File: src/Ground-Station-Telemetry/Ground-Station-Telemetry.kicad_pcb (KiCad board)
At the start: 4 copper layers, 94.9 x 43.2 mm, 47 parts, among them J1 Jumper_NO, P1 3220-20-0200-00, P2 USB, U1 STM32H750VBTx, U2 LMS8117AMP-3.3_NOPB, U3 CP2102-GMR(QFN28), U4 RFM95W-868S2, U5 XB24CDMPIT-001, Y1 ECS-240-18-33-JGN-TR

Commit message: finished initial rev 2 routing
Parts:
- removed H3: Mounting-Hole, Engine-Controller:MountingHole_4.3mm_M4_DIN965
- added C19: 0.1uF, Ground-Station-Telemetry:CAP_0603, F.Cu at (190.5, 82.8)
- added D5: SMBJ36CA-13-F, Ground-Station-Telemetry:CDSOT23-SM712, F.Cu at (207.5, 83.6)
- added D6: SMBJ36CA-13-F, Ground-Station-Telemetry:CDSOT23-SM712, F.Cu at (207.9, 89.2)
- added P3: 54602-908LF, Ground-Station-Telemetry:54602-908LF, F.Cu at (214.6, 86.7)
- added R10: 10, Ground-Station-Telemetry:RES_0603, F.Cu at (200.9, 83.1)
- added R11: 100, Ground-Station-Telemetry:RES_0603, F.Cu at (204.1, 83.7)
- added R12: 10, Ground-Station-Telemetry:RES_0603, F.Cu at (200.9, 85.7)
- added R13: 10, Ground-Station-Telemetry:RES_0603, F.Cu at (200.9, 88.4)
- added R14: 100, Ground-Station-Telemetry:RES_0603, F.Cu at (204.5, 89.0)
- added R15: 10, Ground-Station-Telemetry:RES_0603, F.Cu at (200.9, 90.2)
- added U6: SN65HVD71DR, Ground-Station-Telemetry:SN65HVD71DR, F.Cu at (194.6, 86.9)
- moved R6 30.0 mm to (185.7, 84.8), turned to 180 degrees
- moved D2 29.4 mm to (185.5, 80.9)
- moved R5 13.7 mm to (215.9, 111.8), turned to -90 degrees
- moved R4 10.0 mm to (213.4, 111.8), turned to -90 degrees
- moved C4 8.44 mm to (202.1, 77.4)
- moved R7 8.24 mm to (179.6, 74.3)
- moved D3 7.71 mm to (185.3, 75.3)
- moved C7 7.35 mm to (190.0, 77.7)
- moved U2 7.35 mm to (196.3, 77.0)
- moved P2 4.46 mm to (214.9, 100.2)
- moved C16 3.39 mm to (203.1, 97.4)
- moved C17 3.37 mm to (201.3, 97.4)
- moved D4 3.18 mm to (206.2, 102.5)
- moved U3 2.53 mm to (198.2, 102.1)
- moved R8 2.29 mm to (196.8, 95.4)
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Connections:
- D4 pad 4: 5V -> unconnected-(D4-Pad4)
- D4 pad 5: unconnected-(D4-Pad5) -> 5V
- U1 pad 51: unconnected-(U1-Pad51) -> RS485_RX
- U1 pad 52: unconnected-(U1-Pad52) -> RS485_TX
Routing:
- net RS485_RX: track 0.00 -> 23.2 mm, vias 0 -> 2
- net Y: track 0.00 -> 21.4 mm, vias 0 -> 1
- net RS485_TX: track 0.00 -> 20.0 mm, vias 0 -> 2
- net Z: track 0.00 -> 18.2 mm, vias 0 -> 1
- net B: track 0.00 -> 13.3 mm
- net SWCLK: track 31.3 -> 44.2 mm
- net A: track 0.00 -> 11.5 mm
- net 5V: track 52.5 -> 62.1 mm, vias 1 -> 2
- net SWDIO: track 29.6 -> 37.5 mm
- net 3.3V: track 65.7 -> 72.6 mm, vias 11 -> 14
- net Net-(U6-A): track 0.00 -> 3.75 mm
- net Net-(U6-Y): track 0.00 -> 3.32 mm
- net Net-(U6-Z): track 0.00 -> 3.00 mm
- net Net-(U6-B): track 0.00 -> 2.95 mm
- net Net-(D2-Pad1): track 5.71 -> 3.68 mm
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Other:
- board text added: "A0005 Ground Station Telemetry Rev 2.0"
- board text removed: "A0005 Ground Station Telemetry Rev 1.0"

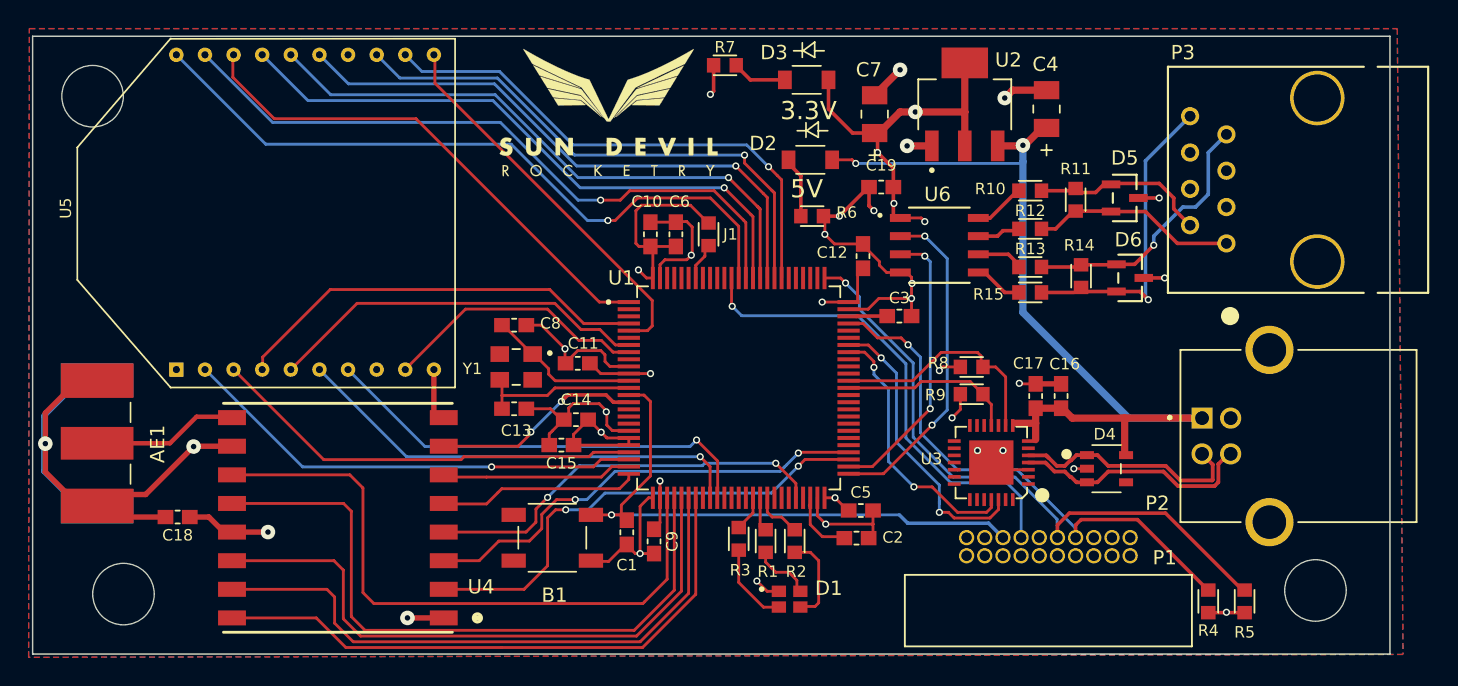
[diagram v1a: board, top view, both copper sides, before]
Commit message: resolved DRC errors
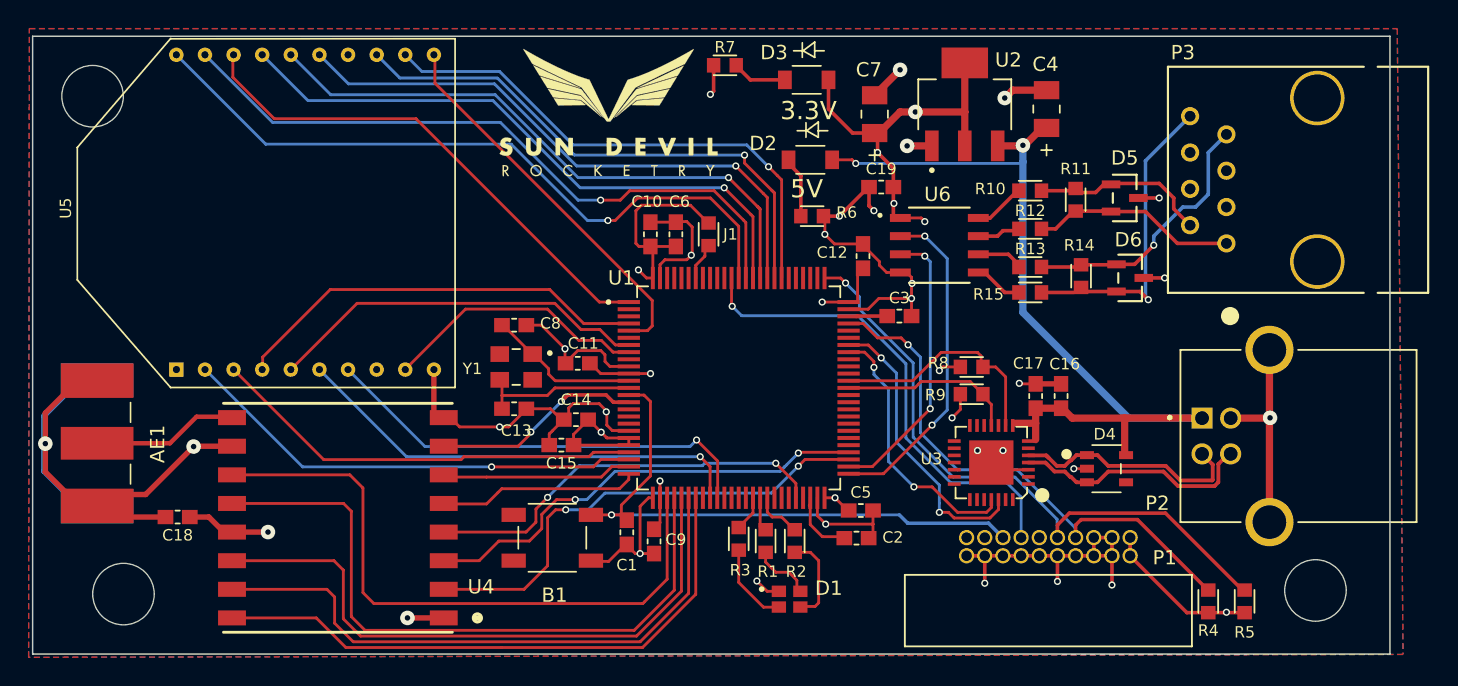
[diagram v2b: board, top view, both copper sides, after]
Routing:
- net Earth: track 128.1 -> 168.1 mm, vias 24 -> 29
- net 3.3V: track 72.6 -> 80.6 mm
